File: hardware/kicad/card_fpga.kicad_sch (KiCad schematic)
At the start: 2 parts, among them J1 Conn_01x13_Socket, U1 LFE5U-25F-6BG381C

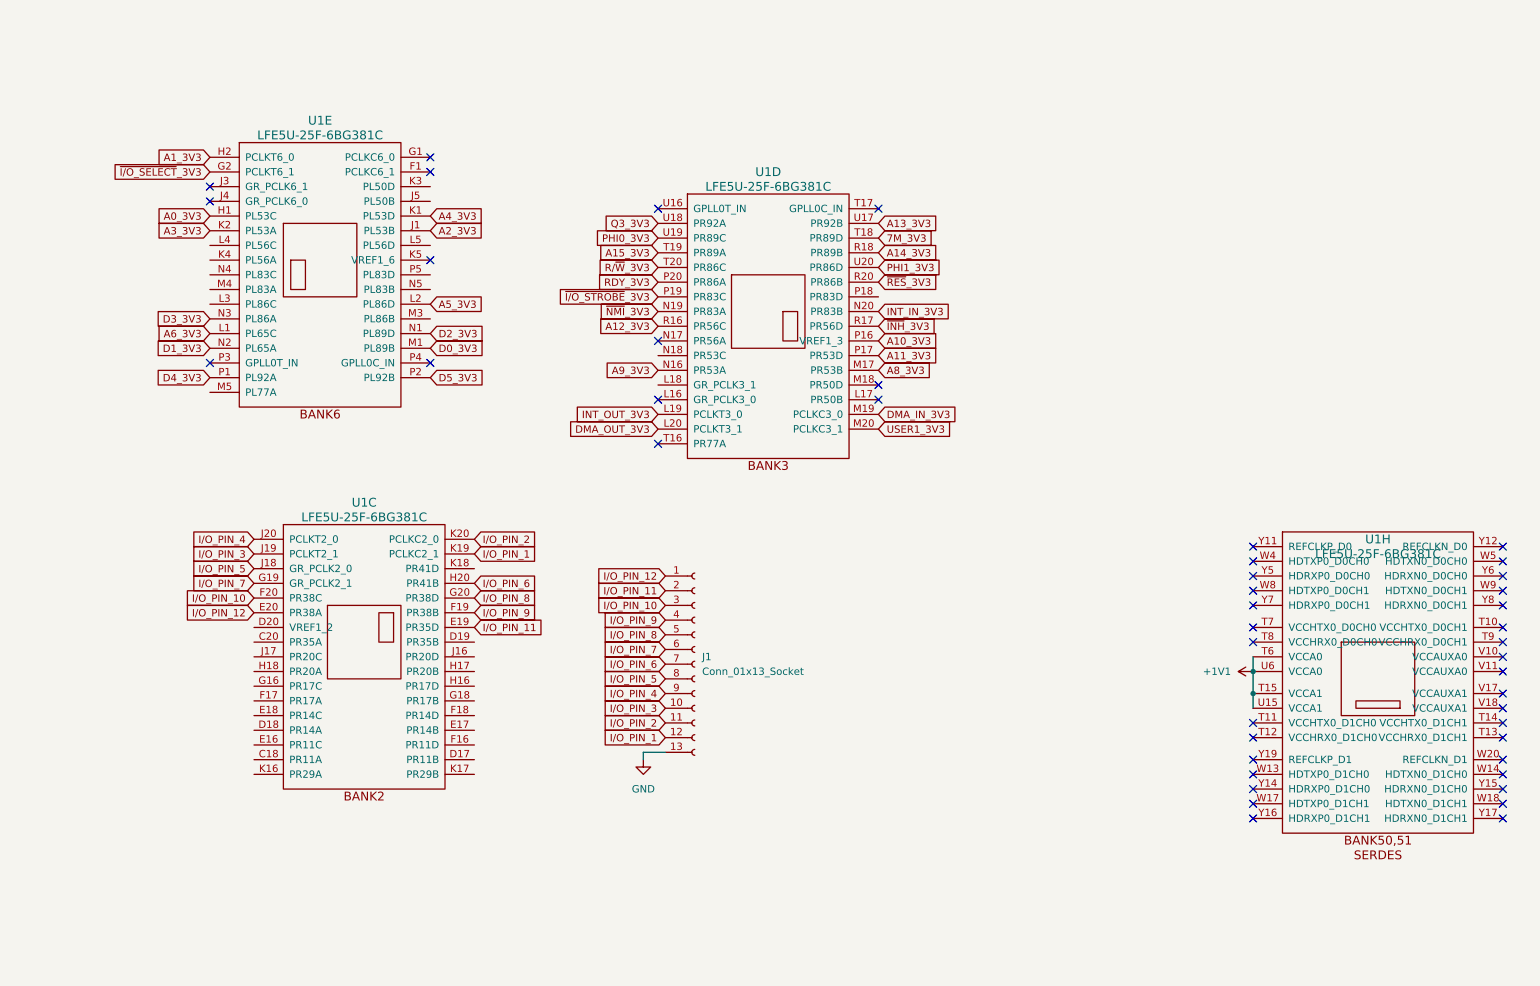
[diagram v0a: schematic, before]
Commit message: Updated Rev. 1.1
- Wired Level Shifters
- Expansion GPIOs
- Oscillator
- Flash
- USB
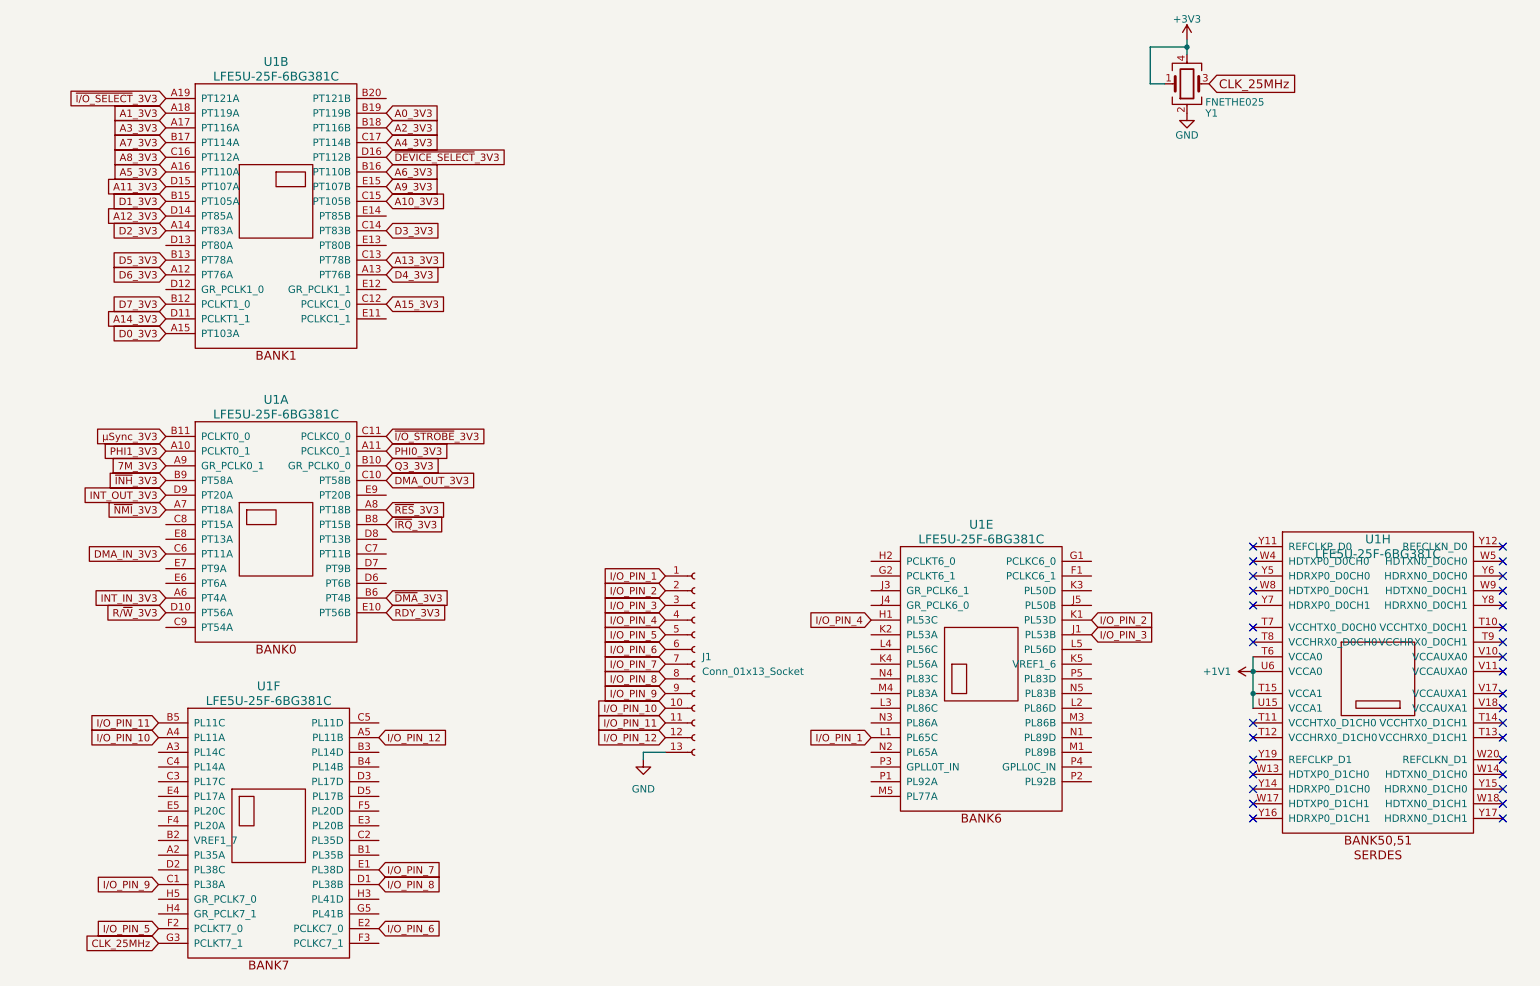
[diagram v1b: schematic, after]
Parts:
- removed unit 3 of U1
- removed unit 4 of U1
- added unit 1 of U1
- added unit 6 of U1
- added unit 2 of U1
- added Y1: FNETHE025, oscxo:Crystal_SMD_7050_4Pads, symbol Device:Crystal_GND24
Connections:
- net 7M_3V3: now also U1.A9 (GR_PCLK0_1)
- net A0_3V3: now also U1.B19 (PT119B); no longer U1.H1 (PL53C)
- net A10_3V3: now also U1.C15 (PT105B)
- net A11_3V3: now also U1.D15 (PT107A)
- net A12_3V3: now also U1.D14 (PT85A)
- net A13_3V3: now also U1.C13 (PT78B)
- net A14_3V3: now also U1.D11 (PCLKT1_1)
- net A15_3V3: now also U1.C12 (PCLKC1_0)
- net A1_3V3: now also U1.A18 (PT119A); no longer U1.H2 (PCLKT6_0)
- net A2_3V3: now also U1.B18 (PT116B); no longer U1.J1 (PL53B)
- net A3_3V3: now also U1.A17 (PT116A); no longer U1.K2 (PL53A)
- net A4_3V3: now also U1.C17 (PT114B); no longer U1.K1 (PL53D)
- net A5_3V3: now also U1.A16 (PT110A); no longer U1.L2 (PL86D)
- net A6_3V3: now also U1.B16 (PT110B); no longer U1.L1 (PL65C)
- net A8_3V3: now also U1.C16 (PT112A)
- net A9_3V3: now also U1.E15 (PT107B)
- net D0_3V3: now also U1.A15 (PT103A); no longer U1.M1 (PL89B)
- net D1_3V3: now also U1.B15 (PT105A); no longer U1.N2 (PL65A)
- net D2_3V3: now also U1.A14 (PT83A); no longer U1.N1 (PL89D)
- net D3_3V3: now also U1.C14 (PT83B); no longer U1.N3 (PL86A)
- net D4_3V3: now also U1.A13 (PT76B); no longer U1.P1 (PL92A)
- net D5_3V3: now also U1.B13 (PT78A); no longer U1.P2 (PL92B)
- net DMA_IN_3V3: now also U1.C6 (PT11A)
- net DMA_OUT_3V3: now also U1.C10 (PT58B)
- net GND: now also Y1.2
- net INT_IN_3V3: now also U1.A6 (PT4A)
- net INT_OUT_3V3: now also U1.D9 (PT20A)
- net I/O_PIN_1: now also J1.1 (Pin_1), U1.L1 (PL65C); no longer J1.12 (Pin_12)
- net I/O_PIN_10: now also J1.10 (Pin_10), U1.A4 (PL11A); no longer J1.3 (Pin_3)
- net I/O_PIN_11: now also J1.11 (Pin_11), U1.B5 (PL11C); no longer J1.2 (Pin_2)
- net I/O_PIN_12: now also J1.12 (Pin_12), U1.A5 (PL11B); no longer J1.1 (Pin_1)
- net I/O_PIN_2: now also J1.2 (Pin_2), U1.K1 (PL53D); no longer J1.11 (Pin_11)
- net I/O_PIN_3: now also J1.3 (Pin_3), U1.J1 (PL53B); no longer J1.10 (Pin_10)
- net I/O_PIN_4: now also J1.4 (Pin_4), U1.H1 (PL53C); no longer J1.9 (Pin_9)
- net I/O_PIN_5: now also J1.5 (Pin_5), U1.F2 (PCLKT7_0); no longer J1.8 (Pin_8)
- net I/O_PIN_6: now also J1.6 (Pin_6), U1.E2 (PCLKC7_0); no longer J1.7 (Pin_7)
- net I/O_PIN_7: now also J1.7 (Pin_7), U1.E1 (PL38D); no longer J1.6 (Pin_6)
- net I/O_PIN_8: now also J1.8 (Pin_8), U1.D1 (PL38B); no longer J1.5 (Pin_5)
- net I/O_PIN_9: now also J1.9 (Pin_9), U1.C1 (PL38A); no longer J1.4 (Pin_4)
- net PHI0_3V3: now also U1.A11 (PCLKC0_1)
- net PHI1_3V3: now also U1.A10 (PCLKT0_1)
- net Q3_3V3: now also U1.B10 (GR_PCLK0_0)
- net RDY_3V3: now also U1.E10 (PT56B)
- net R/~{W}_3V3: now also U1.D10 (PT56A)
- net ~{INH}_3V3: now also U1.B9 (PT58A)
- net ~{I/O_SELECT}_3V3: now also U1.A19 (PT121A); no longer U1.G2 (PCLKT6_1)
- net ~{I/O_STROBE}_3V3: now also U1.C11 (PCLKC0_0)
- net ~{NMI}_3V3: now also U1.A7 (PT18A)
- net ~{RES}_3V3: now also U1.A8 (PT18B)
- new net +3V3: Y1.1, Y1.4
- new net A7_3V3: U1.B17 (PT114A)
- new net CLK_25MHz: U1.G3 (PCLKT7_1), Y1.3
- new net D6_3V3: U1.A12 (PT76A)
- new net D7_3V3: U1.B12 (PCLKT1_0)
- new net ~{DEVICE_SELECT}_3V3: U1.D16 (PT112B)
- new net ~{DMA}_3V3: U1.B6 (PT4B)
- new net ~{IRQ}_3V3: U1.B8 (PT15B)
- new net µSync_3V3: U1.B11 (PCLKT0_0)
- no-connect marks 46 -> 32
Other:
- moved on the sheet: U1E

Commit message: Rev. 1.1
Final Revision - DRC passes
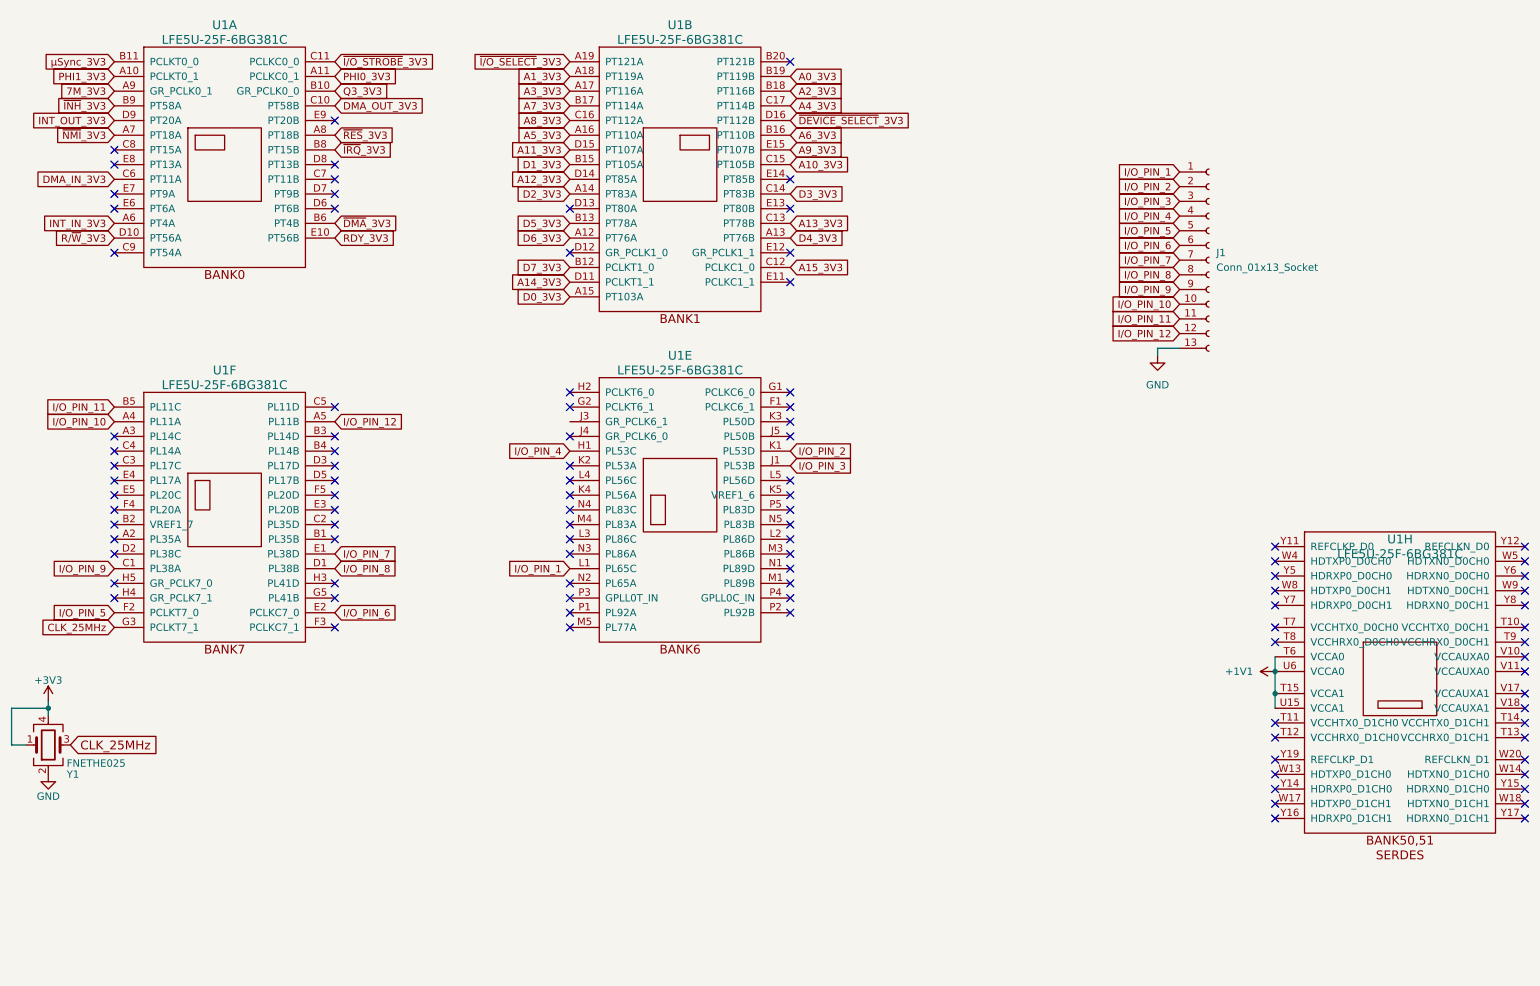
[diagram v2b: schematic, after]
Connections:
- no-connect marks 32 -> 100
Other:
- moved on the sheet: J1, U1A, U1B, U1E, U1F, U1H, Y1

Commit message: Updates FPGA model in BOM and schematics
Replaces LFE5U-25F-6BG381C with LFE5U-85F-8BG381I in multiple files.
Ensures consistency across BOM, schematics, and PCB layouts for the updated FPGA model.
Adjusts related properties such as part number and connectivity attributes.

Addresses a hardware specification upgrade in branch 1.1.
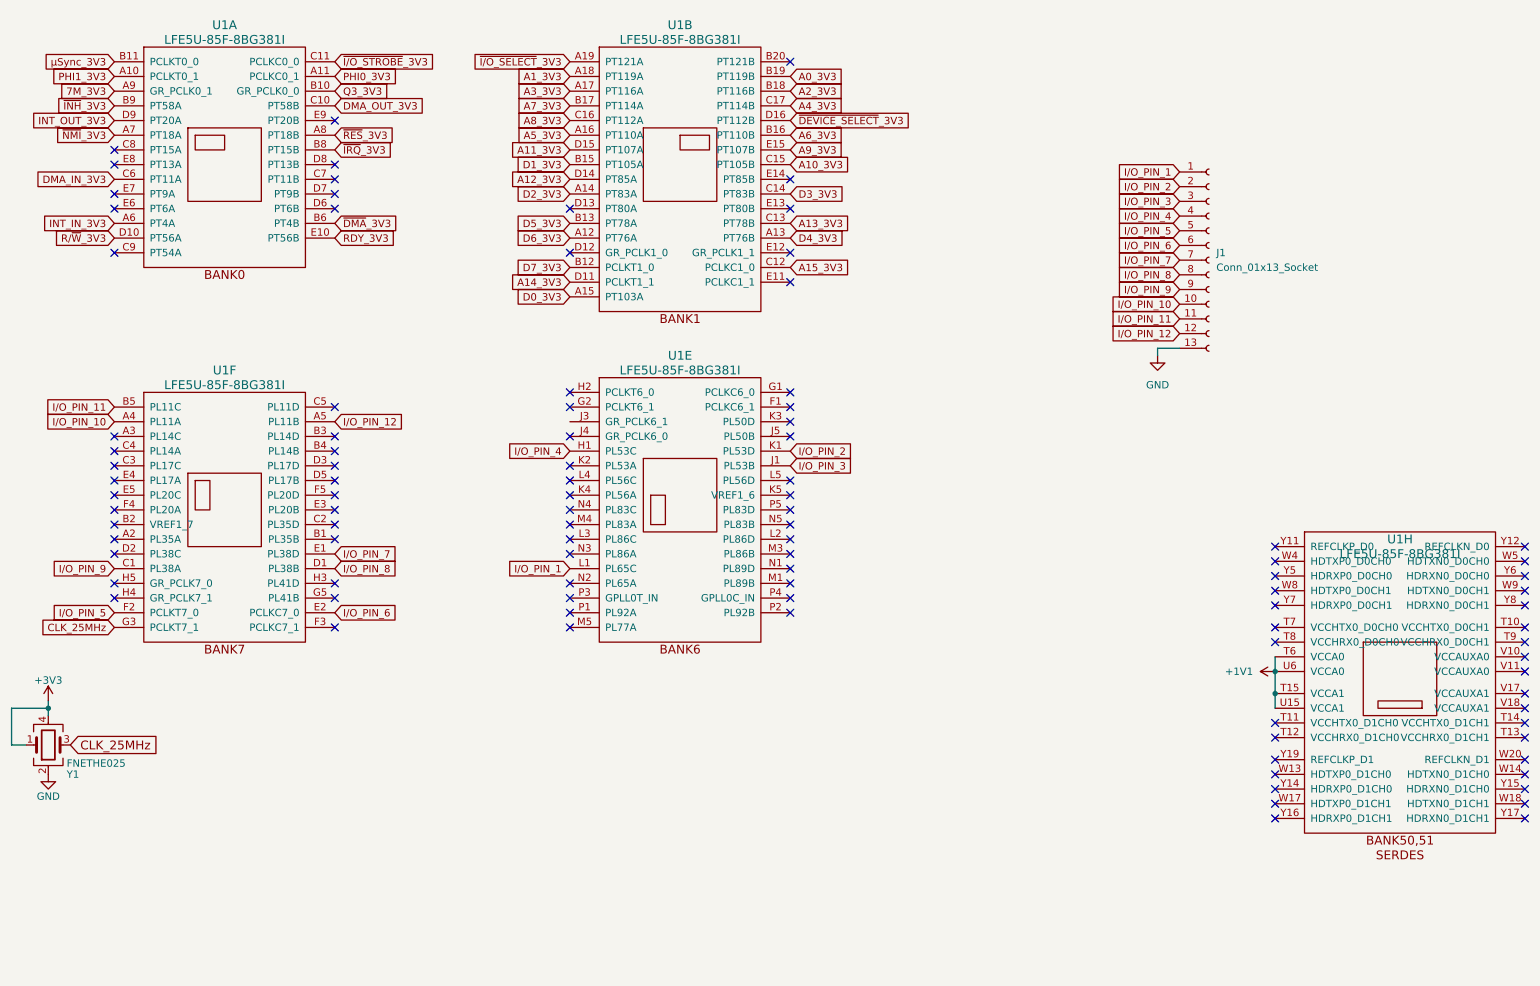
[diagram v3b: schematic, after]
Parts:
- U1: value LFE5U-25F-6BG381C -> LFE5U-85F-8BG381I; MPN LFE5U-85F-6BG381C -> LFE5U-85F-8BG381I
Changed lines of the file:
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@@
 			)
 		)
-		(property "Value" "LFE5U-25F-6BG381C"
+		(property "Value" "LFE5U-85F-8BG381I"
 			(at 53.34 21.59 0)
 			(effects
@@
 			)
 		)
-		(property "MPN" "LFE5U-85F-6BG381C"
+		(property "MPN" "LFE5U-85F-8BG381I"
 			(at 53.34 43.18 0)
 			(effects
@@
 			)
 		)
-		(property "Value" "LFE5U-25F-6BG381C"
+		(property "Value" "LFE5U-85F-8BG381I"
 			(at 53.34 81.28 0)
 			(effects
@@
 			)
 		)
-		(property "MPN" "LFE5U-85F-6BG381C"
+		(property "MPN" "LFE5U-85F-8BG381I"
 			(at 53.34 102.87 0)
 			(effects
@@
 			)
 		)
-		(property "Value" "LFE5U-25F-6BG381C"
+		(property "Value" "LFE5U-85F-8BG381I"
 			(at 256.54 110.49 0)
 			(effects
@@
 			)
 		)
-		(property "MPN" "LFE5U-85F-6BG381C"
+		(property "MPN" "LFE5U-85F-8BG381I"
 			(at 256.54 132.08 0)
 			(effects
@@
 			)
 		)
-		(property "Value" "LFE5U-25F-6BG381C"
+		(property "Value" "LFE5U-85F-8BG381I"
 			(at 132.08 21.59 0)
 			(effects
@@
 			)
 		)
-		(property "MPN" "LFE5U-85F-6BG381C"
+		(property "MPN" "LFE5U-85F-8BG381I"
 			(at 132.08 43.18 0)
 			(effects
@@
 			)
 		)
-		(property "Value" "LFE5U-25F-6BG381C"
+		(property "Value" "LFE5U-85F-8BG381I"
 			(at 132.08 78.74 0)
 			(effects
@@
 			)
 		)
-		(property "MPN" "LFE5U-85F-6BG381C"
+		(property "MPN" "LFE5U-85F-8BG381I"
 			(at 132.08 100.33 0)
 			(effects
